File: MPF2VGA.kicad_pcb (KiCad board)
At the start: 2 copper layers, 99.1 x 99.1 mm, 33 parts, among them IC1 EPM7128SLC84-15, J1 DSUB_HD15, J2 JTAG, U1 MS62256A-35NC, X1 25.175

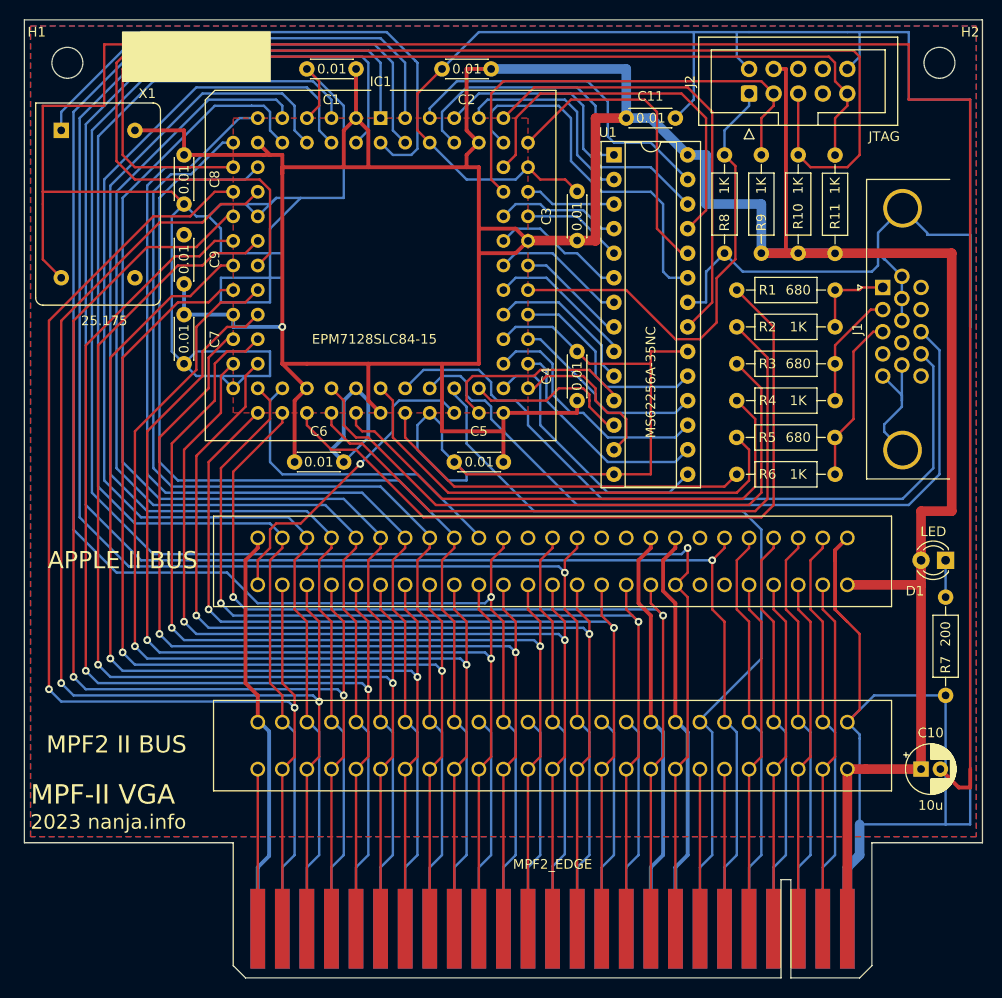
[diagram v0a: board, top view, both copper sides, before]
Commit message: Fix capacitors
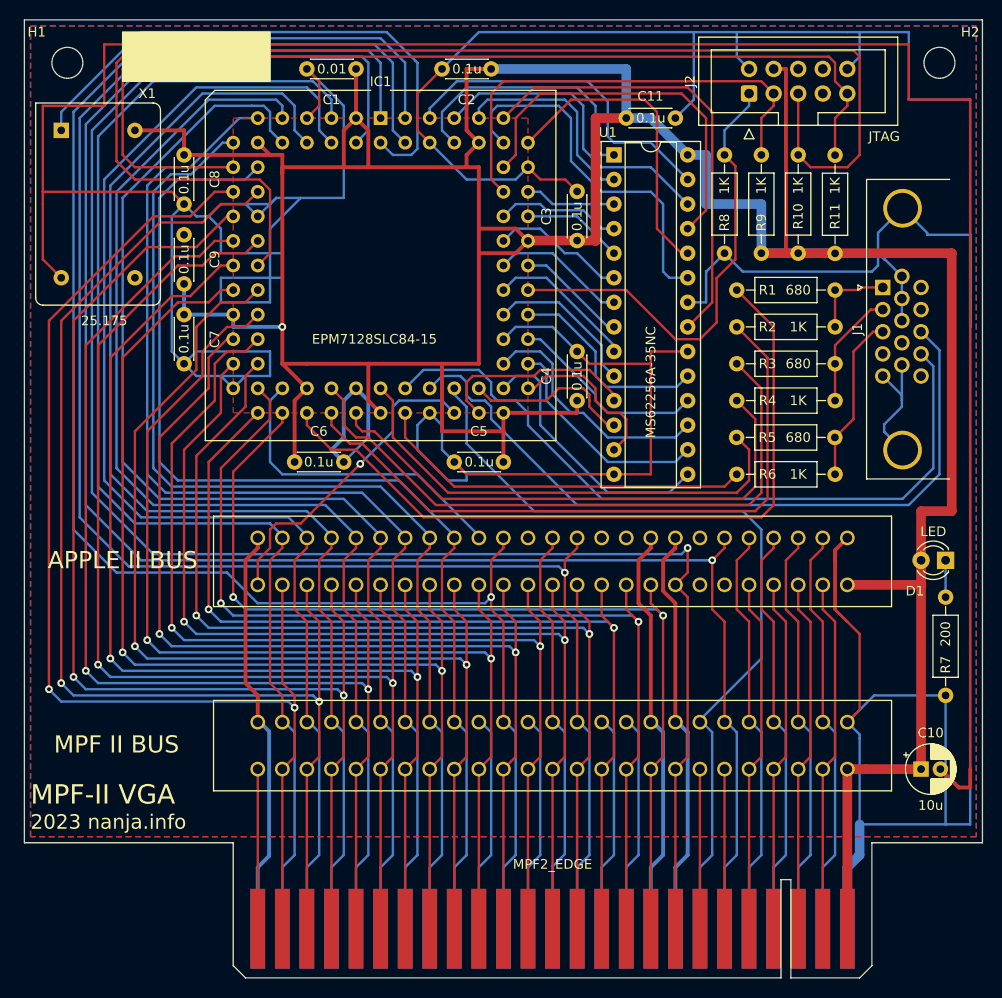
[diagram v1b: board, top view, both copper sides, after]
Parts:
- BUS2: value MPF2 II BUS -> MPF II BUS
- C11, C2, C3, C4, C5, C6, C7, C8, C9: value 0.01 -> 0.1u
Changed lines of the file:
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@@
         (effects (font (size 1 1) (thickness 0.15)))
     )
-    (fp_text value "0.01" (at 2.54 0) (layer "F.SilkS")
+    (fp_text value "0.1u" (at 2.54 0) (layer "F.SilkS")
         (effects (font (size 1 1) (thickness 0.15)))
     )
@@
         (effects (font (size 1 1) (thickness 0.15)))
     )
-    (fp_text value "0.01" (at 2.5 0 90) (layer "F.SilkS")
+    (fp_text value "0.1u" (at 2.5 0 90) (layer "F.SilkS")
         (effects (font (size 1 1) (thickness 0.15)))
     )
@@
         (effects (font (size 1 1) (thickness 0.15)))
     )
-    (fp_text value "0.01" (at 2.54 0 90) (layer "F.SilkS")
+    (fp_text value "0.1u" (at 2.54 0 90) (layer "F.SilkS")
         (effects (font (size 1 1) (thickness 0.15)))
     )
@@
         (effects (font (size 1 1) (thickness 0.15)))
     )
-    (fp_text value "0.01" (at 2.5 0 180) (layer "F.SilkS")
+    (fp_text value "0.1u" (at 2.5 0 180) (layer "F.SilkS")
         (effects (font (size 1 1) (thickness 0.15)))
     )
@@
         (effects (font (size 1 1) (thickness 0.15)))
     )
-    (fp_text value "0.01" (at 2.54 0 -90) (layer "F.SilkS")
+    (fp_text value "0.1u" (at 2.54 0 -90) (layer "F.SilkS")
         (effects (font (size 1 1) (thickness 0.15)))
     )
@@
         (effects (font (size 1 1) (thickness 0.15)))
     )
-    (fp_text value "0.01" (at 2.5 0 -90) (layer "F.SilkS")
+    (fp_text value "0.1u" (at 2.5 0 -90) (layer "F.SilkS")
         (effects (font (size 1 1) (thickness 0.15)))
     )
@@
         (effects (font (size 1 1) (thickness 0.15)))
     )
-    (fp_text value "0.01" (at 2.5 0) (layer "F.SilkS")
+    (fp_text value "0.1u" (at 2.5 0) (layer "F.SilkS")
         (effects (font (size 1 1) (thickness 0.15)))
     )
@@
         (effects (font (size 1.27 1.27) (thickness 0.254)))
     )
-    (fp_text value "MPF2 II BUS" (at -14.605 -2.54) (layer "F.SilkS")
+    (fp_text value "MPF II BUS" (at -14.605 -2.54) (layer "F.SilkS")
         (effects (font (size 1.778 1.778) (thickness 0.254)))
     )
@@
         (effects (font (size 1 1) (thickness 0.15)))
     )
-    (fp_text value "0.01" (at 2.54 0 90) (layer "F.SilkS")
+    (fp_text value "0.1u" (at 2.54 0 90) (layer "F.SilkS")
         (effects (font (size 1 1) (thickness 0.15)))
     )
@@
         (effects (font (size 1 1) (thickness 0.15)))
     )
-    (fp_text value "0.01" (at 2.5 0 180) (layer "F.SilkS")
-        (effects (font (size 1 1) (thickness 0.15)))
-    )
+    (fp_text value "0.1u" (at 2.5 0 180) (layer "F.SilkS")
+        (effects (font (size 1 1) (thickness 0.15)))
+    )
